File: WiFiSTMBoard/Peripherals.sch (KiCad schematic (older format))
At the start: 7 parts

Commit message: added input
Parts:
- added C? (x4): 10n, symbol Device:C_Small
- added R? (x4): 10k, symbol Device:R_Small
- added SW? (x4): SW_MEC_5E, symbol Switch:SW_MEC_5E
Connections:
- net +3V3: now also R?.1, R?.1, R?.1, R?.1
- net GND: now also C?.2, C?.2, C?.2, C?.2, SW?.3 (K), SW?.3 (K), SW?.3 (K), SW?.3 (K), SW?.4 (A), SW?.4 (A), SW?.4 (A), SW?.4 (A)
- new net PB12_BTN: C?.1, R?.2, SW?.1, SW?.2
- new net PB13_BTN: C?.1, R?.2, SW?.1, SW?.2
- new net PB14_BTN: C?.1, R?.2, SW?.1, SW?.2
- new net PB15_BTN: C?.1, R?.2, SW?.1, SW?.2
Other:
- note added: "Communication protocol and GPIO peripherals"
- note added: "GPIO"
- note added: "I2C"
- note added: "SPI"
- note added: "UART"
- note added: "USER BUTTONS"
- note added: "VCC is the value of the power supply \nyou connect to the board. \nNOTE: See the power section of the circuit"
- note removed: "Communication protocol peripherals"
- moved on the sheet: J?, R?

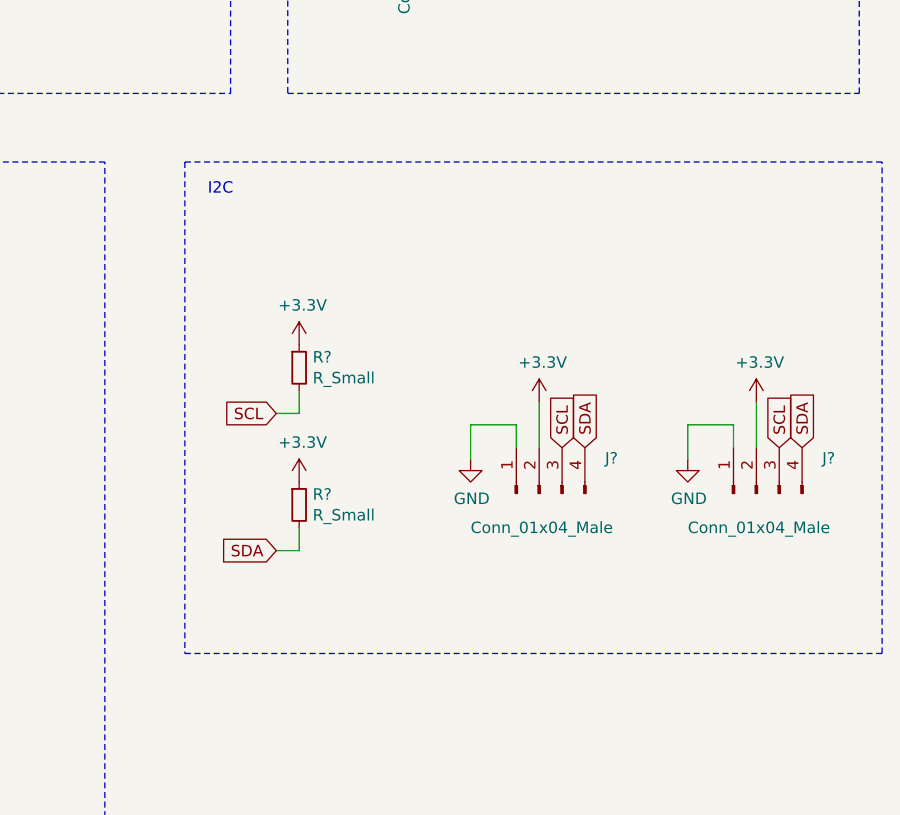
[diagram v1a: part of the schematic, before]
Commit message: added esp8266
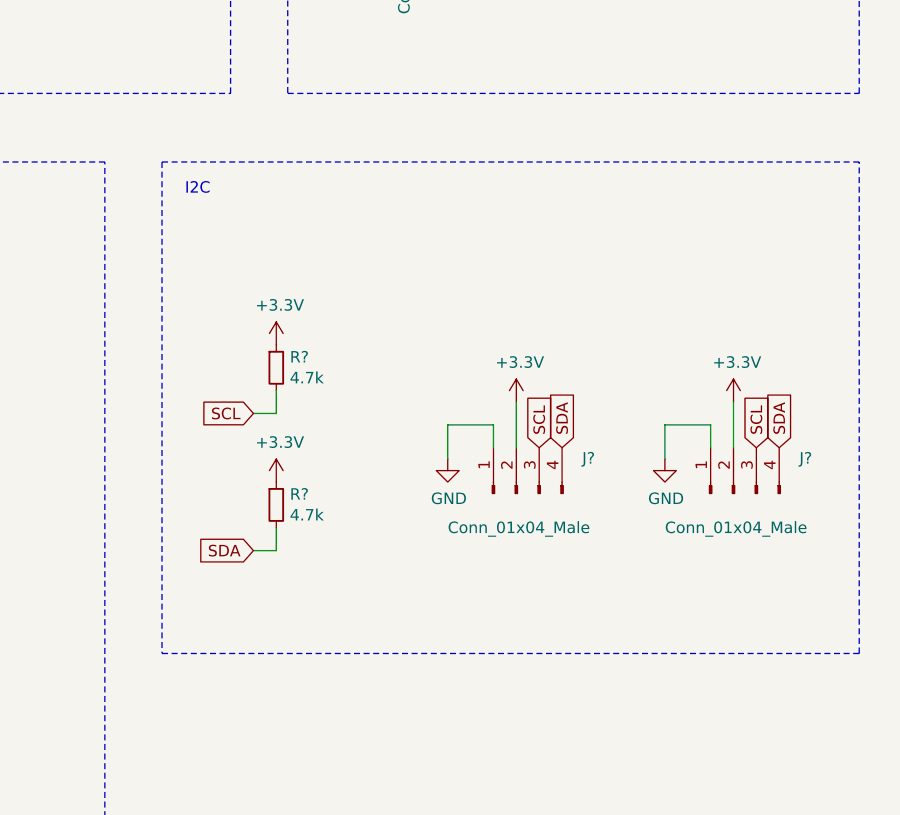
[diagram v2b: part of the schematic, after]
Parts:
- R? (x2): value R_Small -> 4.7k
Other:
- moved on the sheet: J?, R?
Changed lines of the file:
@@
 $Descr User 9843 7874
 encoding utf-8
-Sheet 4 5
+Sheet 4 6
 Title ""
 Date ""
@@
 L Connector:Conn_01x04_Male J?
 U 1 1 619F197C
-P 7600 4300
-F 0 "J?" V 7754 4012 50  0000 R CNN
-F 1 "Conn_01x04_Male" V 7450 4600 50  0000 R CNN
-F 2 "" H 7600 4300 50  0001 C CNN
-F 3 "~" H 7600 4300 50  0001 C CNN
-	1    7600 4300
+P 7500 4300
+F 0 "J?" V 7654 4012 50  0000 R CNN
+F 1 "Conn_01x04_Male" V 7350 4600 50  0000 R CNN
+F 2 "" H 7500 4300 50  0001 C CNN
+F 3 "~" H 7500 4300 50  0001 C CNN
+	1    7500 4300
 	0    -1   -1   0
 $EndComp
@@
 L power:+3.3V #PWR?
 U 1 1 619FA27E
-P 7600 3900
-F 0 "#PWR?" H 7600 3750 50  0001 C CNN
-F 1 "+3.3V" H 7615 4073 50  0000 C CNN
-F 2 "" H 7600 3900 50  0001 C CNN
-F 3 "" H 7600 3900 50  0001 C CNN
-	1    7600 3900
-	1    0    0    -1
-$EndComp
-Wire Wire Line
-	7600 4100 7600 3900
+P 7500 3900
+F 0 "#PWR?" H 7500 3750 50  0001 C CNN
+F 1 "+3.3V" H 7515 4073 50  0000 C CNN
+F 2 "" H 7500 3900 50  0001 C CNN
+F 3 "" H 7500 3900 50  0001 C CNN
+	1    7500 3900
+	1    0    0    -1
+$EndComp
+Wire Wire Line
+	7500 4100 7500 3900
 $Comp
 L power:GND #PWR?
 U 1 1 619FAC3E
-P 7300 4150
-F 0 "#PWR?" H 7300 3900 50  0001 C CNN
-F 1 "GND" H 7305 3977 50  0000 C CNN
-F 2 "" H 7300 4150 50  0001 C CNN
-F 3 "" H 7300 4150 50  0001 C CNN
-	1    7300 4150
-	1    0    0    -1
-$EndComp
-Wire Wire Line
-	7500 4100 7500 4000
-Wire Wire Line
-	7500 4000 7300 4000
-Wire Wire Line
-	7300 4000 7300 4150
-Text GLabel 7700 4100 1    50   Input ~ 0
+P 7200 4150
+F 0 "#PWR?" H 7200 3900 50  0001 C CNN
+F 1 "GND" H 7205 3977 50  0000 C CNN
+F 2 "" H 7200 4150 50  0001 C CNN
+F 3 "" H 7200 4150 50  0001 C CNN
+	1    7200 4150
+	1    0    0    -1
+$EndComp
+Wire Wire Line
+	7400 4100 7400 4000
+Wire Wire Line
+	7400 4000 7200 4000
+Wire Wire Line
+	7200 4000 7200 4150
+Text GLabel 7600 4100 1    50   Input ~ 0
 SCL
-Text GLabel 6450 4550 0    50   Input ~ 0
+Text GLabel 6350 4550 0    50   Input ~ 0
 SDA
 $Comp
 L Connector:Conn_01x04_Male J?
 U 1 1 619FD71A
-P 8550 4300
-F 0 "J?" V 8704 4012 50  0000 R CNN
-F 1 "Conn_01x04_Male" V 8400 4600 50  0000 R CNN
-F 2 "" H 8550 4300 50  0001 C CNN
-F 3 "~" H 8550 4300 50  0001 C CNN
-	1    8550 4300
+P 8450 4300
+F 0 "J?" V 8604 4012 50  0000 R CNN
+F 1 "Conn_01x04_Male" V 8300 4600 50  0000 R CNN
+F 2 "" H 8450 4300 50  0001 C CNN
+F 3 "~" H 8450 4300 50  0001 C CNN
+	1    8450 4300
 	0    -1   -1   0
 $EndComp
@@
 L power:+3.3V #PWR?
 U 1 1 619FD720
-P 8550 3900
-F 0 "#PWR?" H 8550 3750 50  0001 C CNN
-F 1 "+3.3V" H 8565 4073 50  0000 C CNN
-F 2 "" H 8550 3900 50  0001 C CNN
-F 3 "" H 8550 3900 50  0001 C CNN
-	1    8550 3900
-	1    0    0    -1
-$EndComp
-Wire Wire Line
-	8550 4100 8550 3900
+P 8450 3900
+F 0 "#PWR?" H 8450 3750 50  0001 C CNN
+F 1 "+3.3V" H 8465 4073 50  0000 C CNN
+F 2 "" H 8450 3900 50  0001 C CNN
+F 3 "" H 8450 3900 50  0001 C CNN
+	1    8450 3900
+	1    0    0    -1
+$EndComp
+Wire Wire Line
+	8450 4100 8450 3900
 $Comp
 L power:GND #PWR?
 U 1 1 619FD727
-P 8250 4150
-F 0 "#PWR?" H 8250 3900 50  0001 C CNN
-F 1 "GND" H 8255 3977 50  0000 C CNN
-F 2 "" H 8250 4150 50  0001 C CNN
-F 3 "" H 8250 4150 50  0001 C CNN
-	1    8250 4150
-	1    0    0    -1
-$EndComp
-Wire Wire Line
-	8450 4100 8450 4000
-Wire Wire Line
-	8450 4000 8250 4000
-Wire Wire Line
-	8250 4000 8250 4150
+P 8150 4150
+F 0 "#PWR?" H 8150 3900 50  0001 C CNN
+F 1 "GND" H 8155 3977 50  0000 C CNN
+F 2 "" H 8150 4150 50  0001 C CNN
+F 3 "" H 8150 4150 50  0001 C CNN
+	1    8150 4150
+	1    0    0    -1
+$EndComp
+Wire Wire Line
+	8350 4100 8350 4000
+Wire Wire Line
+	8350 4000 8150 4000
+Wire Wire Line
+	8150 4000 8150 4150
+Text GLabel 8550 4100 1    50   Input ~ 0
+SCL
 Text GLabel 8650 4100 1    50   Input ~ 0
-SCL
-Text GLabel 8750 4100 1    50   Input ~ 0
 SDA
-Text GLabel 6450 3950 0    50   Input ~ 0
+Text GLabel 6350 3950 0    50   Input ~ 0
 SCL
 $Comp
 L Device:R_Small R?
 U 1 1 619FDAFC
-P 6550 3750
-F 0 "R?" H 6609 3796 50  0000 L CNN
-F 1 "R_Small" H 6609 3705 50  0000 L CNN
-F 2 "" H 6550 3750 50  0001 C CNN
-F 3 "~" H 6550 3750 50  0001 C CNN
-	1    6550 3750
+P 6450 3750
+F 0 "R?" H 6509 3796 50  0000 L CNN
+F 1 "4.7k" H 6509 3705 50  0000 L CNN
+F 2 "" H 6450 3750 50  0001 C CNN
+F 3 "~" H 6450 3750 50  0001 C CNN
+	1    6450 3750
 	1    0    0    -1
 $EndComp
@@
 L Device:R_Small R?
 U 1 1 619FE055
-P 6550 4350
-F 0 "R?" H 6609 4396 50  0000 L CNN
-F 1 "R_Small" H 6609 4305 50  0000 L CNN
-F 2 "" H 6550 4350 50  0001 C CNN
-F 3 "~" H 6550 4350 50  0001 C CNN
-	1    6550 4350
-	1    0    0    -1
-$EndComp
-Wire Wire Line
-	6450 3950 6550 3950
-Wire Wire Line
-	6550 3950 6550 3850
-Wire Wire Line
-	6450 4550 6550 4550
-Wire Wire Line
-	6550 4550 6550 4450
+P 6450 4350
+F 0 "R?" H 6509 4396 50  0000 L CNN
+F 1 "4.7k" H 6509 4305 50  0000 L CNN
+F 2 "" H 6450 4350 50  0001 C CNN
+F 3 "~" H 6450 4350 50  0001 C CNN
+	1    6450 4350
+	1    0    0    -1
+$EndComp
+Wire Wire Line
+	6350 3950 6450 3950
+Wire Wire Line
+	6450 3950 6450 3850
+Wire Wire Line
+	6350 4550 6450 4550
+Wire Wire Line
+	6450 4550 6450 4450
 $Comp
 L power:+3.3V #PWR?
 U 1 1 619FE9C2
-P 6550 3650
-F 0 "#PWR?" H 6550 3500 50  0001 C CNN
-F 1 "+3.3V" H 6565 3823 50  0000 C CNN
-F 2 "" H 6550 3650 50  0001 C CNN
-F 3 "" H 6550 3650 50  0001 C CNN
-	1    6550 3650
+P 6450 3650
+F 0 "#PWR?" H 6450 3500 50  0001 C CNN
+F 1 "+3.3V" H 6465 3823 50  0000 C CNN
+F 2 "" H 6450 3650 50  0001 C CNN
+F 3 "" H 6450 3650 50  0001 C CNN
+	1    6450 3650
 	1    0    0    -1
 $EndComp
@@
 L power:+3.3V #PWR?
 U 1 1 619FEDE0
-P 6550 4250
-F 0 "#PWR?" H 6550 4100 50  0001 C CNN
-F 1 "+3.3V" H 6565 4423 50  0000 C CNN
-F 2 "" H 6550 4250 50  0001 C CNN
-F 3 "" H 6550 4250 50  0001 C CNN
-	1    6550 4250
-	1    0    0    -1
-$EndComp
-Text GLabel 7800 4100 1    50   Input ~ 0
+P 6450 4250
+F 0 "#PWR?" H 6450 4100 50  0001 C CNN
+F 1 "+3.3V" H 6465 4423 50  0000 C CNN
+F 2 "" H 6450 4250 50  0001 C CNN
+F 3 "" H 6450 4250 50  0001 C CNN
+	1    6450 4250
+	1    0    0    -1
+$EndComp
+Text GLabel 7700 4100 1    50   Input ~ 0
 SDA
 $Comp
@@
 GPIO
 Wire Notes Line
-	6050 2850 6050 5000
-Wire Notes Line
-	6050 5000 9100 5000
-Wire Notes Line
-	9100 5000 9100 2850
-Wire Notes Line
-	6050 2850 9100 2850
-Text Notes 6150 3000 0    50   ~ 0
+	5950 2850 5950 5000
+Wire Notes Line
+	5950 5000 9000 5000
+Wire Notes Line
+	9000 5000 9000 2850
+Wire Notes Line
+	5950 2850 9000 2850
+Text Notes 6050 3000 0    50   ~ 0
 I2C
 Wire Notes Line

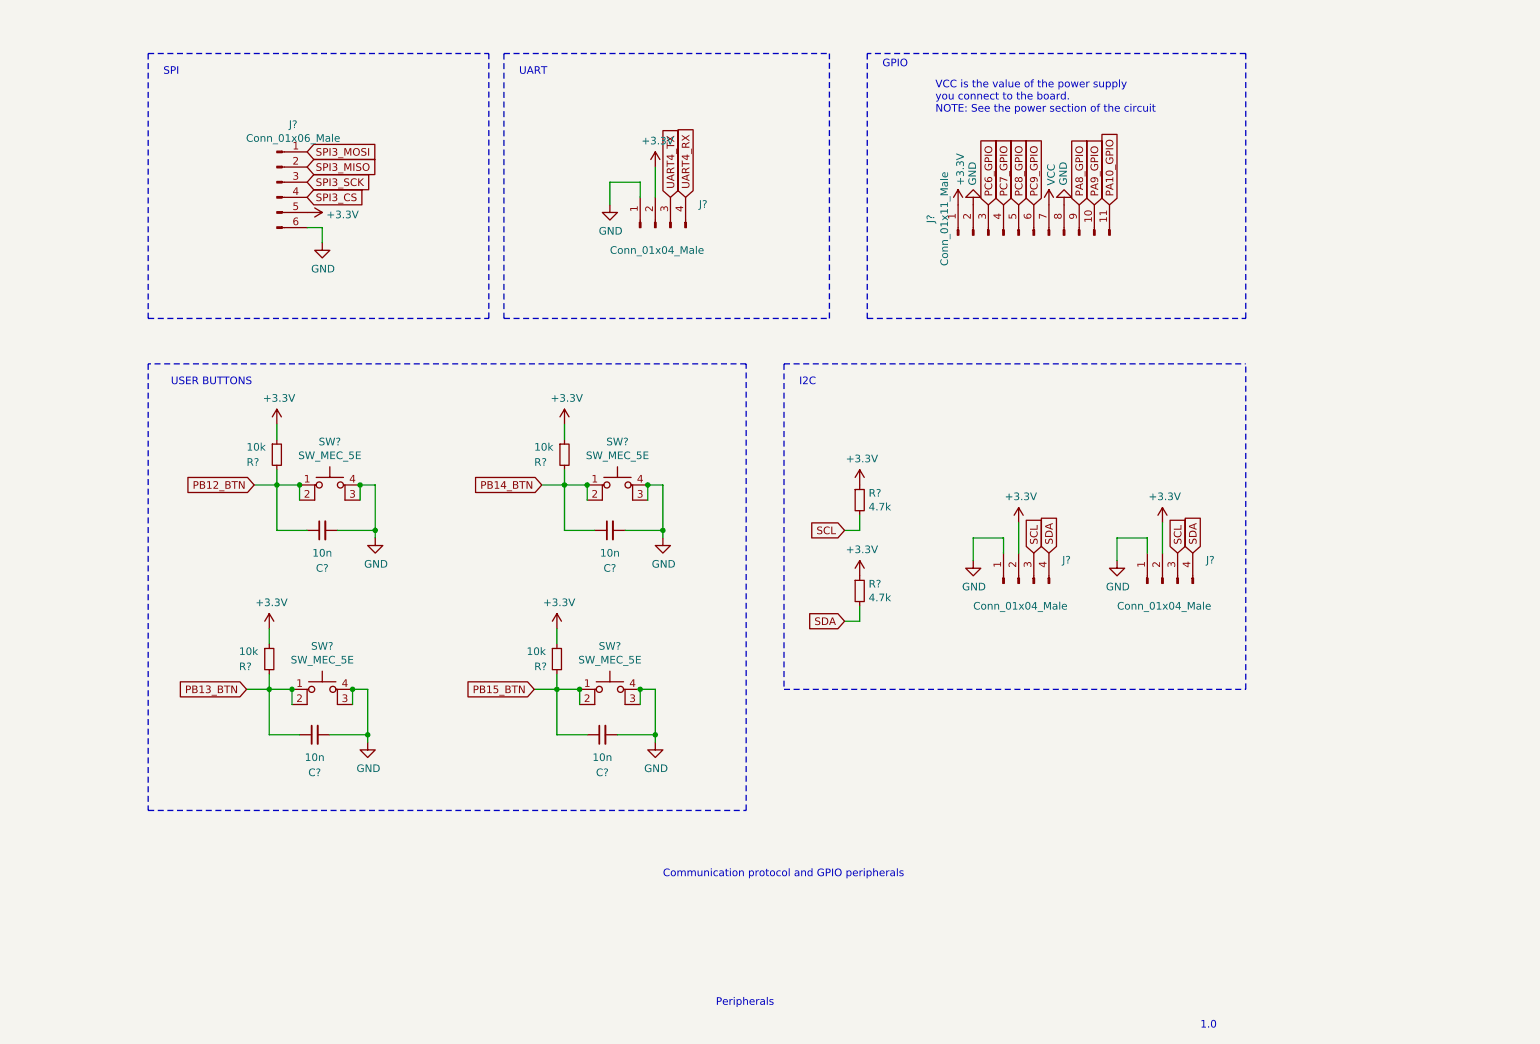
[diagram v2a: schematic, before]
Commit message: finished serial circuit
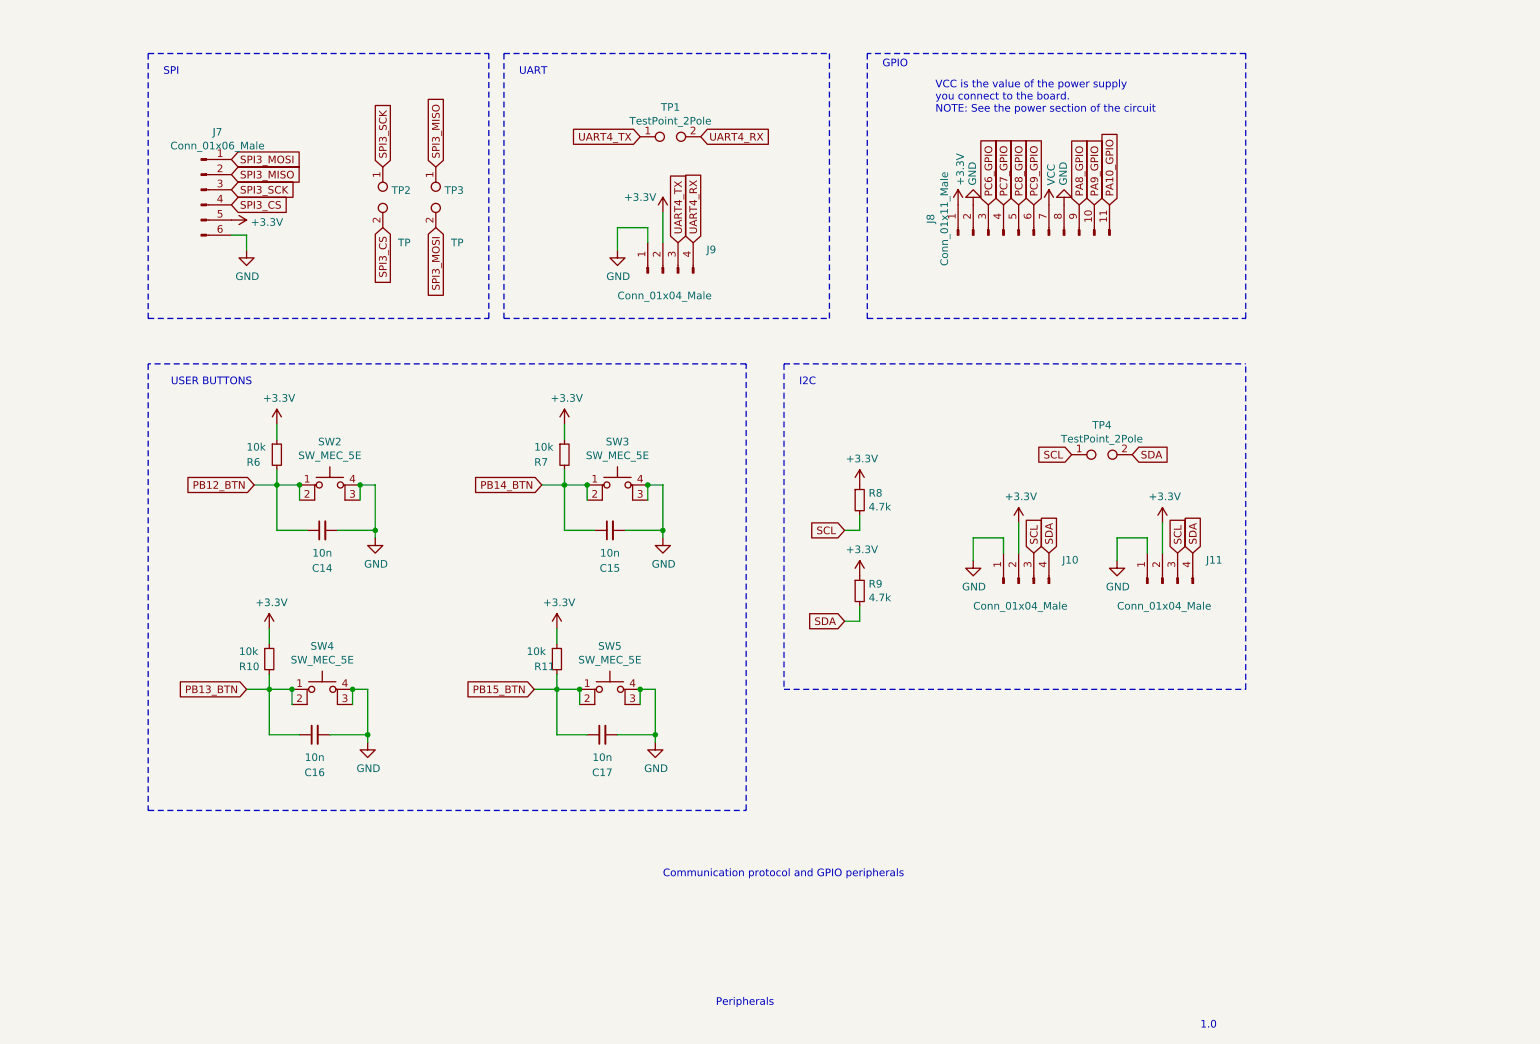
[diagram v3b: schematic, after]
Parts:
- added TP1, TP4: TestPoint_2Pole, symbol Connector:TestPoint_2Pole
- added TP2, TP3: TP, symbol Connector:TestPoint_2Pole
- gave numbers to parts that had none: 19
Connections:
- net SCL: now also TP4.1
- net SDA: now also TP4.2
- net SPI3_CS: now also TP2.2
- net SPI3_MISO: now also TP3.1
- net SPI3_MOSI: now also TP3.2
- net SPI3_SCK: now also TP2.1
- net UART4_RX: now also TP1.2
- net UART4_TX: now also TP1.1
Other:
- moved on the sheet: J7, J9

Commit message: starting PCB layout
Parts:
- removed J7: Conn_01x06_Male, symbol Connector:Conn_01x06_Male
- removed SW2, SW3, SW4, SW5: SW_MEC_5E, symbol Switch:SW_MEC_5E
- removed TP1, TP4: TestPoint_2Pole, symbol Connector:TestPoint_2Pole
- removed TP2, TP3: TP, symbol Connector:TestPoint_2Pole
- added J12: Conn_01x04_Male, Connector_Molex:Molex_KK-396_A-41791-0004_1x04_P3.96mm_Vertical, symbol Connector:Conn_01x04_Male
- added J7: SWD, Connector_PinHeader_2.54mm:PinHeader_2x05_P2.54mm_Vertical, symbol Connector_Generic:Conn_02x05_Odd_Even
- added J9: Conn_01x06_Male, Connector_PinHeader_2.54mm:PinHeader_1x06_P2.54mm_Vertical, symbol Connector:Conn_01x06_Male
- added R6: 22, Resistor_SMD:R_0603_1608Metric, symbol Device:R_Small
- added SW2: PB12, Button_Switch_SMD:SW_Push_1P1T_NO_6x6mm_H9.5mm, symbol Switch:SW_Push_Dual_x2
- added SW3: PB14, Button_Switch_SMD:SW_Push_1P1T_NO_6x6mm_H9.5mm, symbol Switch:SW_Push_Dual_x2
- added SW4: PB13, Button_Switch_SMD:SW_Push_1P1T_NO_6x6mm_H9.5mm, symbol Switch:SW_Push_Dual_x2
- added SW5: PB15, Button_Switch_SMD:SW_Push_1P1T_NO_6x6mm_H9.5mm, symbol Switch:SW_Push_Dual_x2
- added TP10: RX3_TP, TestPoint:TestPoint_Pad_D2.0mm, symbol Connector:TestPoint
- added TP11: SCL_TP, TestPoint:TestPoint_Pad_D2.0mm, symbol Connector:TestPoint
- added TP12: SDA_TP, TestPoint:TestPoint_Pad_D2.0mm, symbol Connector:TestPoint
- added TP7: TX4_TP, TestPoint:TestPoint_Pad_D2.0mm, symbol Connector:TestPoint
- added TP8: RX4_TP, TestPoint:TestPoint_Pad_D2.0mm, symbol Connector:TestPoint
- added TP9: TX3_TP, TestPoint:TestPoint_Pad_D2.0mm, symbol Connector:TestPoint
- C14, C15, C16, C17: footprint (none) -> Capacitor_SMD:C_0603_1608Metric
- J10: renamed from J8; footprint (none) -> Connector_PinHeader_2.54mm:PinHeader_1x11_P2.54mm_Vertical
- J11: renamed from J9; footprint (none) -> Connector_Molex:Molex_KK-396_A-41791-0004_1x04_P3.96mm_Vertical
- J13: renamed from J10; footprint (none) -> Connector_Molex:Molex_KK-396_A-41791-0004_1x04_P3.96mm_Vertical
- J14: renamed from J11; footprint (none) -> Connector_Molex:Molex_KK-396_A-41791-0004_1x04_P3.96mm_Vertical
- R10: renamed from R9; footprint (none) -> Resistor_SMD:R_0805_2012Metric
- R11: renamed from R10; footprint (none) -> Resistor_SMD:R_0805_2012Metric
- R12: renamed from R11; footprint (none) -> Resistor_SMD:R_0805_2012Metric
- R7: renamed from R6; footprint (none) -> Resistor_SMD:R_0805_2012Metric
- R8: renamed from R7; footprint (none) -> Resistor_SMD:R_0805_2012Metric
- R9: renamed from R8; footprint (none) -> Resistor_SMD:R_0805_2012Metric
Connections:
- net +3V3: now also J12.2 (Pin_2), J7.1 (Pin_1), J9.5 (Pin_5)
- net GND: now also J12.1 (Pin_1), J7.3 (Pin_3), J7.5 (Pin_5), J7.9 (Pin_9), J9.6 (Pin_6), SW2.2 (D), SW3.2 (D), SW4.2 (D), SW5.2 (D)
- net PB12_BTN: now also SW2.1 (C)
- net PB13_BTN: now also SW4.1 (C)
- net PB14_BTN: now also SW3.1 (C)
- net PB15_BTN: now also SW5.1 (C)
- net SCL: now also TP11.1
- net SDA: now also TP12.1
- net UART4_RX: now also TP8.1
- net UART4_TX: now also TP7.1
- new net: J7.2 (Pin_2), R6.1
- new net NRST: J7.10 (Pin_10)
- new net PA4_GPIO: J9.1 (Pin_1)
- new net PA5_GPIO: J9.2 (Pin_2)
- new net PA6_GPIO: J9.3 (Pin_3)
- new net PA7_GPIO: J9.4 (Pin_4)
- new net SWCLK: J7.4 (Pin_4)
- new net SWDIO: R6.2
- new net SWO: J7.6 (Pin_6)
- new net USART3_RX: J12.4 (Pin_4), TP10.1
- new net USART3_TX: J12.3 (Pin_3), TP9.1
- no-connect marks 0 -> 2
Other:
- note added: "SWD Connector"
- note added: "UART3"
- note added: "UART4"
- note removed: "SPI"
- note removed: "UART"
- moved on the sheet: C14, C15, C16, C17, J10, J11, J13, J14, R10, R11, R12, R7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

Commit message: .
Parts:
- removed J11, J13: Conn_01x04_Male, Connector_Molex:Molex_KK-396_A-41791-0004_1x04_P3.96mm_Vertical, symbol Connector:Conn_01x04_Male
- removed J9: Conn_01x06_Male, Connector_PinHeader_2.54mm:PinHeader_1x06_P2.54mm_Vertical, symbol Connector:Conn_01x06_Male
- removed TP7: TX4_TP, TestPoint:TestPoint_Pad_D2.0mm, symbol Connector:TestPoint
- removed TP8: RX4_TP, TestPoint:TestPoint_Pad_D2.0mm, symbol Connector:TestPoint
- J12, J14: footprint Connector_Molex:Molex_KK-396_A-41791-0004_1x04_P3.96mm_Vertical -> Connector_PinHeader_2.54mm:PinHeader_1x04_P2.54mm_Horizontal
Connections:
- net PA8_GPIO is gone; now on net GND: J10.9 (Pin_9)
- net VCC is gone; now on net +3V3: J10.7 (Pin_7)
- net +3V3: no longer J10.1 (Pin_1)
- net GND: no longer J10.2 (Pin_2)
- net SCL: now also J14.4 (Pin_4); no longer J14.3 (Pin_3)
- net SDA: now also J14.3 (Pin_3); no longer J14.4 (Pin_4)
- net USART3_RX: now also J12.3 (Pin_3); no longer J12.4 (Pin_4)
- net USART3_TX: now also J12.4 (Pin_4); no longer J12.3 (Pin_3)
- net PA10_GPIO: no longer names the net of J10.11 (Pin_11)
- net PA9_GPIO: no longer names the net of J10.10 (Pin_10)
- net PB12_BTN renamed PA3_BTN
- net PB13_BTN renamed PA4_BTN
- net PB14_BTN renamed PA5_BTN
- net PB15_BTN renamed PA6_BTN
- net PC6_GPIO renamed PC15
- net PC7_GPIO renamed PB6_GPIO
- net PC8_GPIO renamed PB5_GPIO
- net PC9_GPIO renamed PB4_GPIO
- new net PC13: J10.1 (Pin_1)
- new net PC14: J10.2 (Pin_2)
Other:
- note removed: "UART4"
- moved on the sheet: J14
